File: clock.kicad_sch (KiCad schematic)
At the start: 44 parts, among them J1 USB_C_Receptacle_USB2.0_16P, J2 Conn_01x02_Pin, J3 Conn_01x02_Pin, J4 Conn_01x02_Pin, J5 Battery, SW1 SW_Push, SW2 SW_Push, SW3 SW_Push, U1 STM32F072CBT6, U2 USBLC6-2SC6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

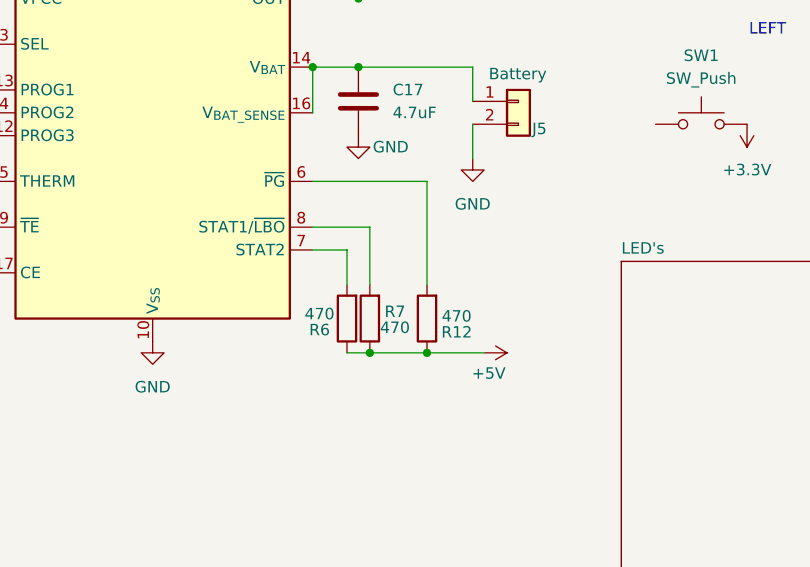
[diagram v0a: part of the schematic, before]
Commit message: deleted some resistors
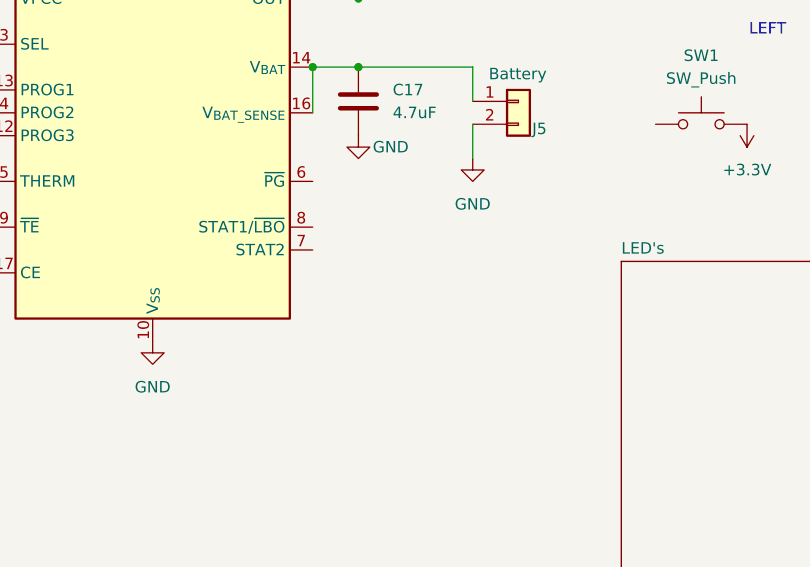
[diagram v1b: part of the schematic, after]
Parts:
- removed R12, R6, R7: 470, symbol Device:R

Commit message: pull up resistor
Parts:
- added R6: 5.1kR, symbol Device:R
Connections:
- net +5V: now also R6.2
- net LBO: now reaches U4.7 (STAT2)
- net LBO: now also R6.1
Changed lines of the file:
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@@
 	)
 	(junction
+		(at 161.29 115.57)
+		(diameter 0)
+		(color 0 0 0 0)
+	)
+	(junction
 		(at 127 63.5)
 		(diameter 0)
@@
 	(wire
 		(pts
+			(xy 154.94 110.49) (xy 154.94 115.57)
+		)
+		(stroke
+			(width 0)
+			(type default)
+		)
+	)
+	(wire
+		(pts
 			(xy 118.11 82.55) (xy 109.22 82.55)
 		)
@@
 	(wire
 		(pts
+			(xy 153.67 110.49) (xy 154.94 110.49)
+		)
+		(stroke
+			(width 0)
+			(type default)
+		)
+	)
+	(wire
+		(pts
 			(xy 124.46 31.75) (xy 129.54 31.75)
 		)
@@
 	(wire
 		(pts
+			(xy 161.29 115.57) (xy 173.99 115.57)
+		)
+		(stroke
+			(width 0)
+			(type default)
+		)
+	)
+	(wire
+		(pts
 			(xy 109.22 82.55) (xy 109.22 77.47)
 		)
@@
 	(wire
 		(pts
+			(xy 173.99 115.57) (xy 173.99 114.3)
+		)
+		(stroke
+			(width 0)
+			(type default)
+		)
+	)
+	(wire
+		(pts
 			(xy 44.45 107.95) (xy 50.8 107.95)
 		)
@@
 	(wire
 		(pts
+			(xy 154.94 115.57) (xy 161.29 115.57)
+		)
+		(stroke
+			(width 0)
+			(type default)
+		)
+	)
+	(wire
+		(pts
 			(xy 262.89 26.67) (xy 262.89 27.94)
 		)
@@
 		)
 	)
+	(global_label "LBO"
+		(shape input)
+		(at 173.99 114.3 0)
+		(fields_autoplaced yes)
+		(effects
+			(font
+				(size 1.27 1.27)
+			)
+			(justify left)
+		)
+		(property "Intersheetrefs" "${INTERSHEET_REFS}"
+			(at 180.6038 114.3 0)
+			(effects
+				(font
+					(size 1.27 1.27)
+				)
+				(justify left)
+				(hide yes)
+			)
+		)
+	)
 	(global_label "BOOT"
 		(shape input)
@@
 	)
 	(symbol
+		(lib_id "power:+5V")
+		(at 161.29 123.19 180)
+		(unit 1)
+		(exclude_from_sim no)
+		(in_bom yes)
+		(on_board yes)
+		(dnp no)
+		(fields_autoplaced yes)
+		(property "Reference" "#PWR021"
+			(at 161.29 119.38 0)
+			(effects
+				(font
+					(size 1.27 1.27)
+				)
+				(hide yes)
+			)
+		)
+		(property "Value" "+5V"
+			(at 161.29 128.27 0)
+			(effects
+				(font
+					(size 1.27 1.27)
+				)
+			)
+		)
+		(property "Footprint" ""
+			(at 161.29 123.19 0)
+			(effects
+				(font
+					(size 1.27 1.27)
+				)
+				(hide yes)
+			)
+		)
+		(property "Datasheet" ""
+			(at 161.29 123.19 0)
+			(effects
+				(font
+					(size 1.27 1.27)
+				)
+				(hide yes)
+			)
+		)
+		(property "Description" "Power symbol creates a global label with name \"+5V\""
+			(at 161.29 123.19 0)
+			(effects
+				(font
+					(size 1.27 1.27)
+				)
+				(hide yes)
+			)
+		)
+		(pin "1"
+		)
+		(instances
+			(project ""
+				(path "/959d2641-02eb-4caa-b1c6-84a86321825f"
+					(reference "#PWR021")
+					(unit 1)
+				)
+			)
+		)
+	)
+	(symbol
 		(lib_id "Device:C")
 		(at 66.04 104.14 0)
@@
 					(unit 1)
 				)
+			)
+		)
+	)
+	(symbol
+		(lib_id "Device:R")
+		(at 161.29 119.38 0)
+		(unit 1)
+		(exclude_from_sim no)
+		(in_bom yes)
+		(on_board yes)
+		(dnp no)
+		(fields_autoplaced yes)
+		(property "Reference" "R6"
+			(at 163.83 118.1099 0)
+			(effects
+				(font
+					(size 1.27 1.27)
+				)
+				(justify left)
+			)
+		)
+		(property "Value" "5.1kR"
+			(at 163.83 120.6499 0)
+			(effects
+				(font
+					(size 1.27 1.27)
+				)
+				(justify left)
+			)
+		)
+		(property "Footprint" ""
+			(at 159.512 119.38 90)
+			(effects
+				(font
+					(size 1.27 1.27)
+				)
+				(hide yes)
+			)
+		)
+		(property "Datasheet" "~"
+			(at 161.29 119.38 0)
+			(effects
+				(font
+					(size 1.27 1.27)
+				)
+				(hide yes)
+			)
+		)
+		(property "Description" "Resistor"
+			(at 161.29 119.38 0)
+			(effects
+				(font
+					(size 1.27 1.27)
+				)
+				(hide yes)
+			)
+		)
+		(pin "1"
+		)
+		(pin "2"
+		)
+		(instances
+			(project ""
+				(path "/959d2641-02eb-4caa-b1c6-84a86321825f"
+					(reference "R6")
+					(unit 1)
+				)

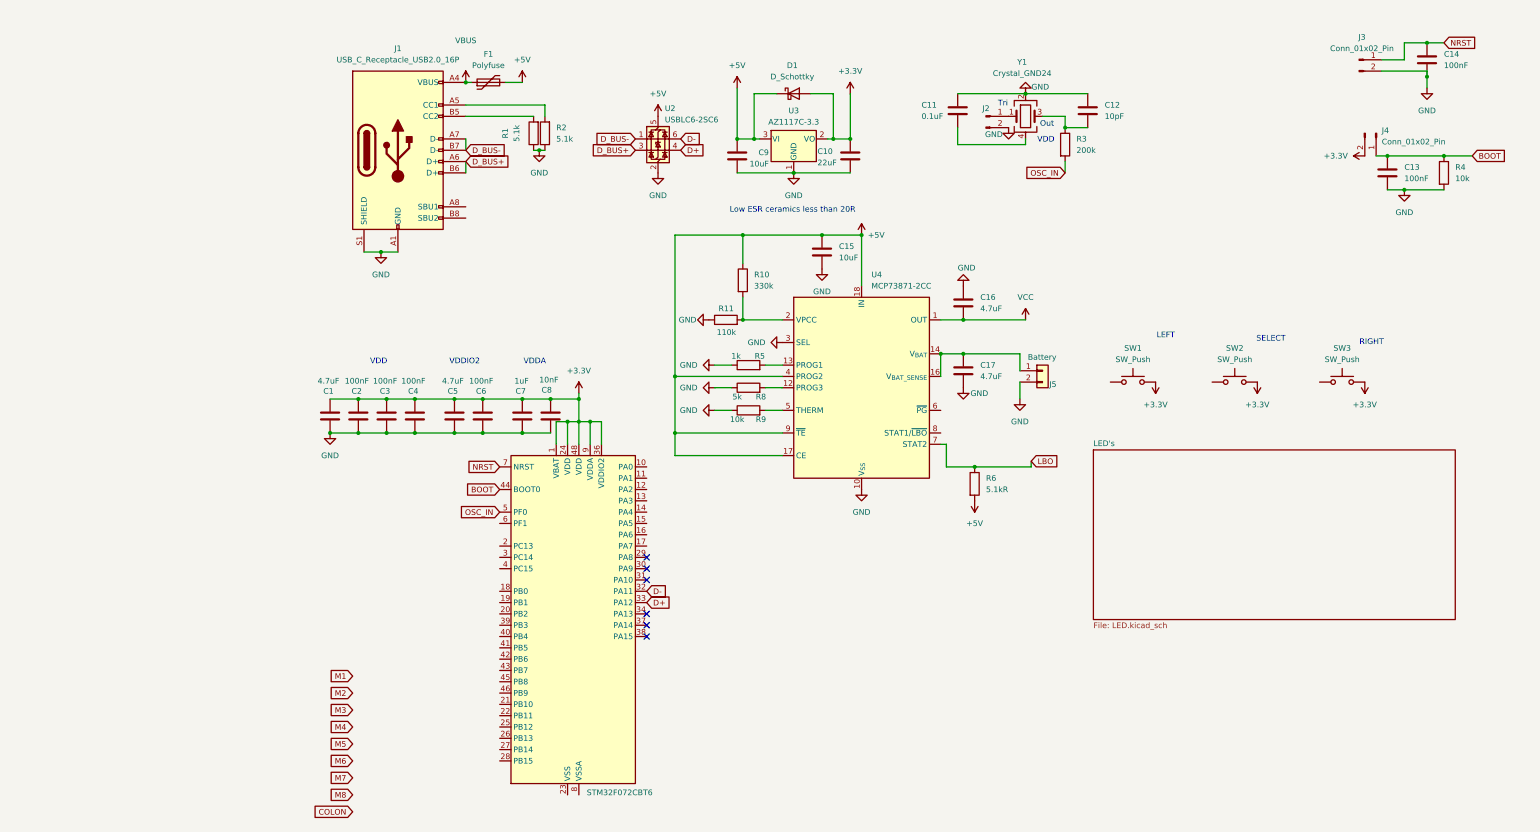
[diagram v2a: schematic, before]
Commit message: lots of changes, circuit to disable chip now works (Ihope)
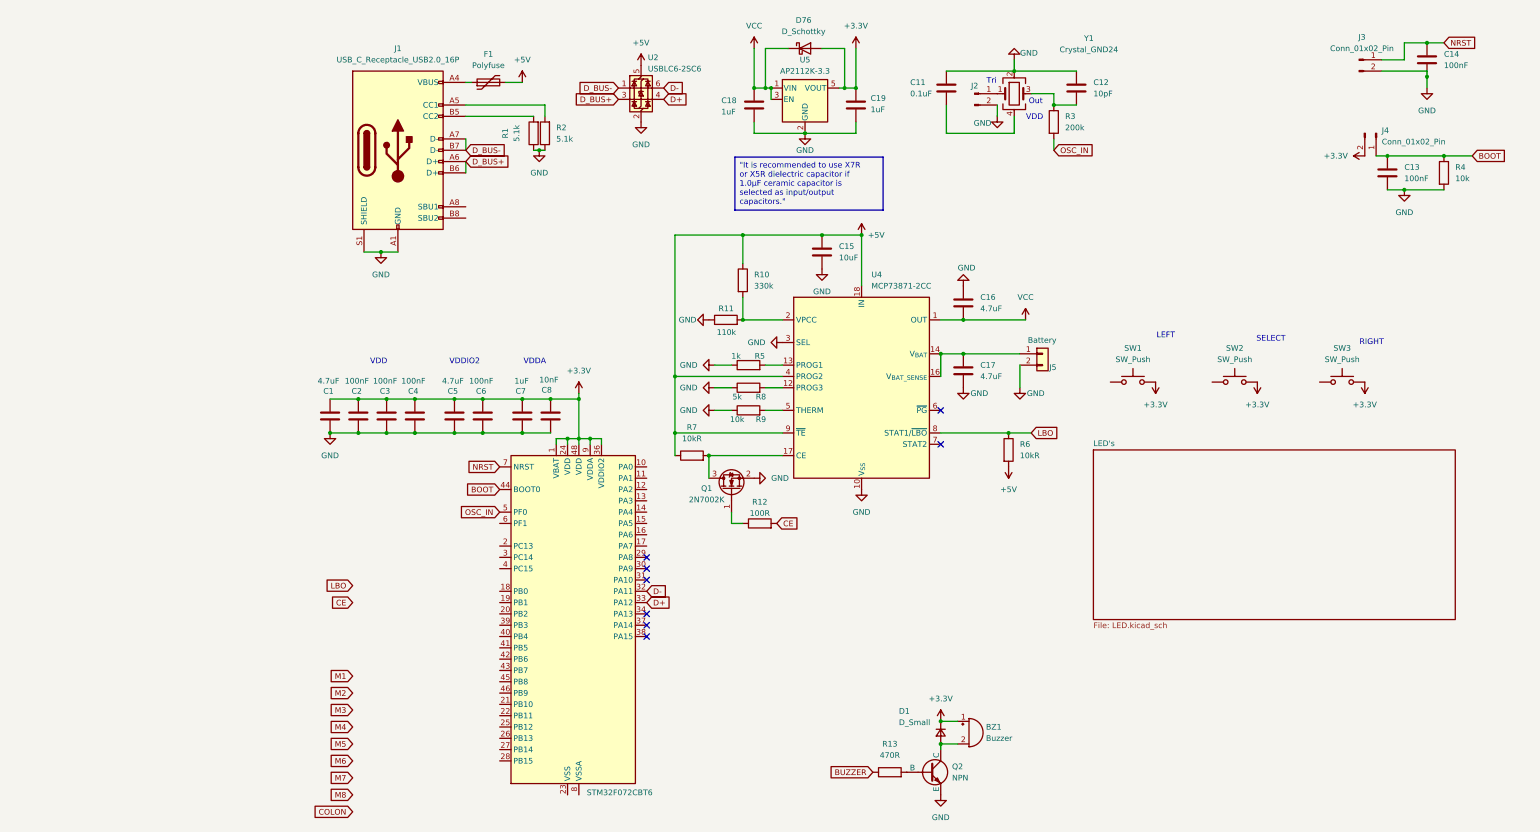
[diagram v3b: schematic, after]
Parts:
- removed C10: 22uF, Capacitor_SMD:C_0805_2012Metric_Pad1.18x1.45mm_HandSolder, symbol Device:C
- removed C9: 10uF, Capacitor_SMD:C_0805_2012Metric_Pad1.18x1.45mm_HandSolder, symbol Device:C
- removed D1: D_Schottky, Diode_SMD:D_SOD-123F, symbol Device:D_Schottky
- removed U3: AZ1117C-3.3, Package_TO_SOT_SMD:SOT-89-3_Handsoldering, symbol Regulator_Linear:AZ1117-3.3
- added BZ1: Buzzer, symbol Device:Buzzer
- added C18, C19: 1uF, Capacitor_SMD:C_0805_2012Metric_Pad1.18x1.45mm_HandSolder, symbol Device:C
- added D1: D_Small, symbol Device:D_Small
- added D76: D_Schottky, Diode_SMD:D_SOD-123F, symbol Device:D_Schottky
- added Q1: 2N7002K, Package_TO_SOT_SMD:SOT-23, symbol Transistor_FET:2N7002K
- added Q2: NPN, symbol Simulation_SPICE:NPN
- added R12: 100R, symbol Device:R
- added R13: 470R, symbol Device:R
- added R7: 10kR, symbol Device:R
- added U5: AP2112K-3.3, Package_TO_SOT_SMD:SOT-23-5, symbol Regulator_Linear:AP2112K-3.3
- R6: value 5.1kR -> 10kR
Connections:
- net +3.3V: now also BZ1.1 (+), C19.1, D1.1 (K), D76.2 (A), U5.5 (VOUT)
- net +5V: now also R7.1; no longer U4.17 (CE)
- net GND: now also C18.2, C19.2, Q1.2 (S), Q2.3 (E), U5.2 (GND)
- net LBO: now also U4.8 (STAT1/~{LBO}); no longer U4.7 (STAT2)
- net VCC: now also C18.1, D76.1 (K), U5.1 (VIN), U5.3 (EN)
- net VBUS: no longer names the net of F1.1, J1.A4 (VBUS), J1.A9 (VBUS), J1.B4 (VBUS), J1.B9 (VBUS)
- new net: BZ1.2 (-), D1.2 (A), Q2.1 (C)
- new net: Q1.1 (G), R12.1
- new net: Q2.2 (B), R13.2
- new net: Q1.3 (D), R7.2, U4.17 (CE)
- new net BUZZER: R13.1
- new net CE: R12.2
- no-connect marks 6 -> 8
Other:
- note removed: "Low ESR ceramics less than 20R"
- moved on the sheet: C11, C12, J2, J5, R3, R6, U2, Y1

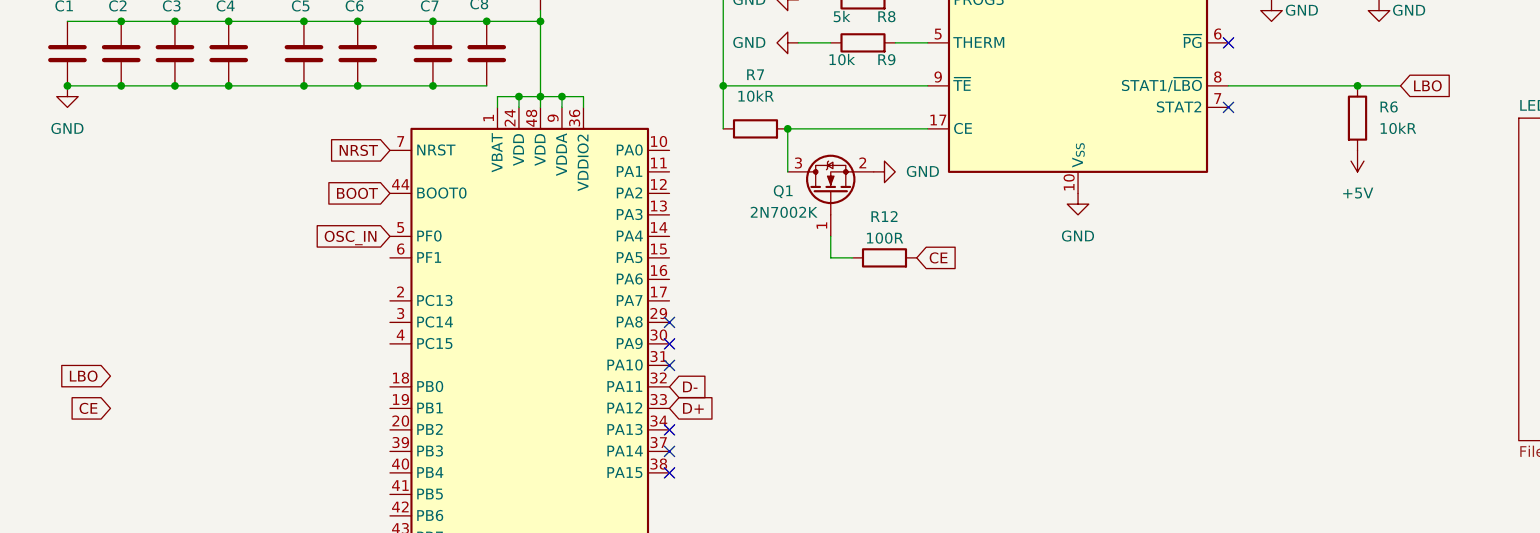
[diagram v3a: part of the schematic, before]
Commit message: st files + voltage divider
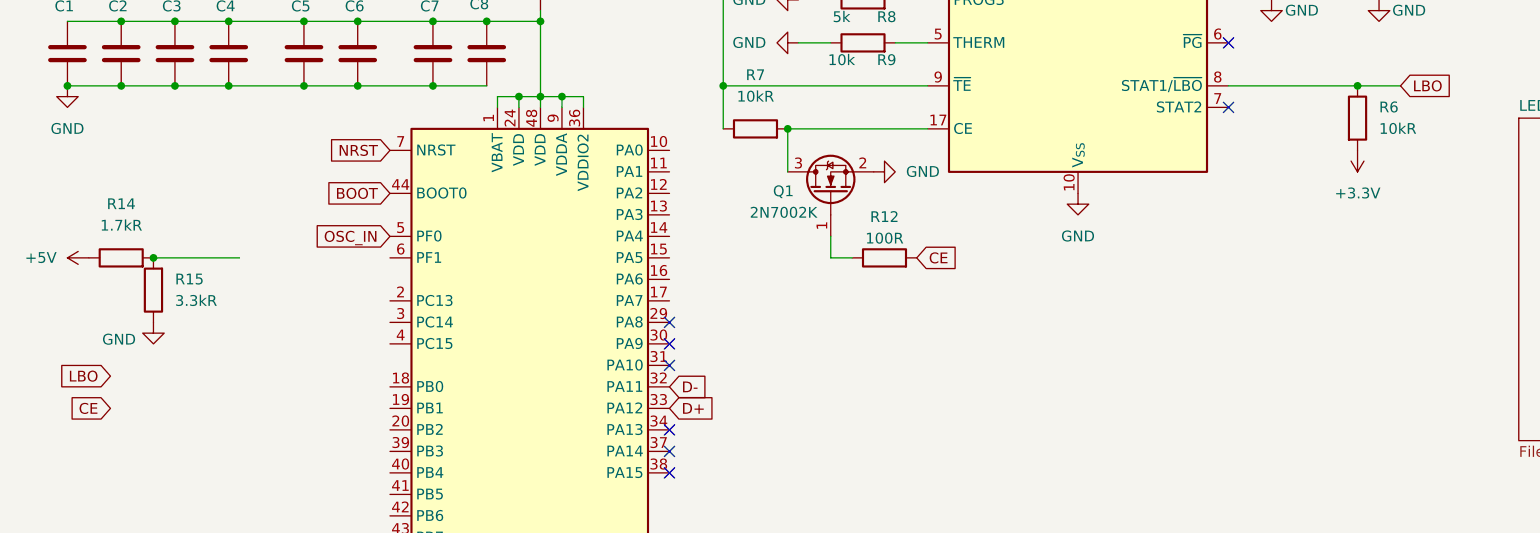
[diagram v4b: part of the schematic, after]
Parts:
- added R14: 1.7kR, symbol Device:R
- added R15: 3.3kR, symbol Device:R
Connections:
- net +3.3V: now also R6.2
- net +5V: now also R14.1; no longer R6.2
- net GND: now also R15.1
- new net: R14.2, R15.2
